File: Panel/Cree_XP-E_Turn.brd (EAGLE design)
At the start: 32 x 20 mm, 5 parts

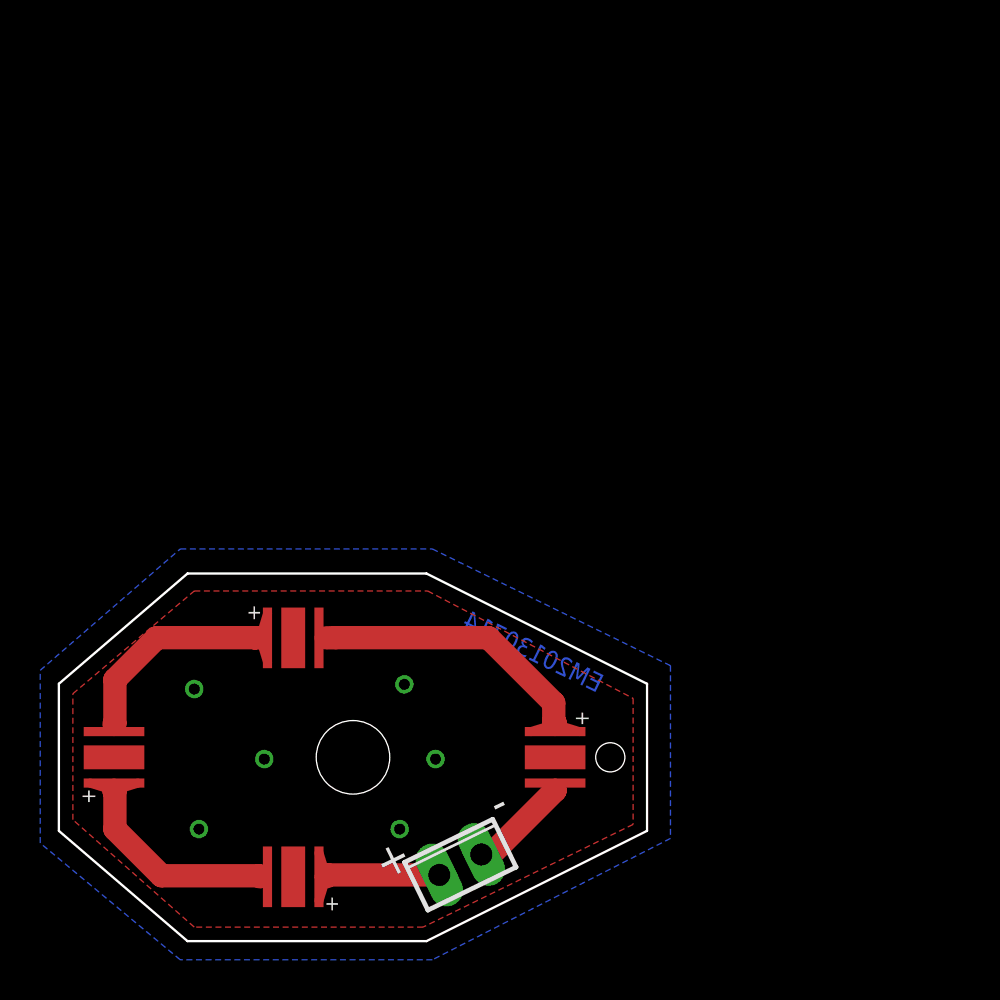
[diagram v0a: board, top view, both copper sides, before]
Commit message: Used Updated XP-E footprint
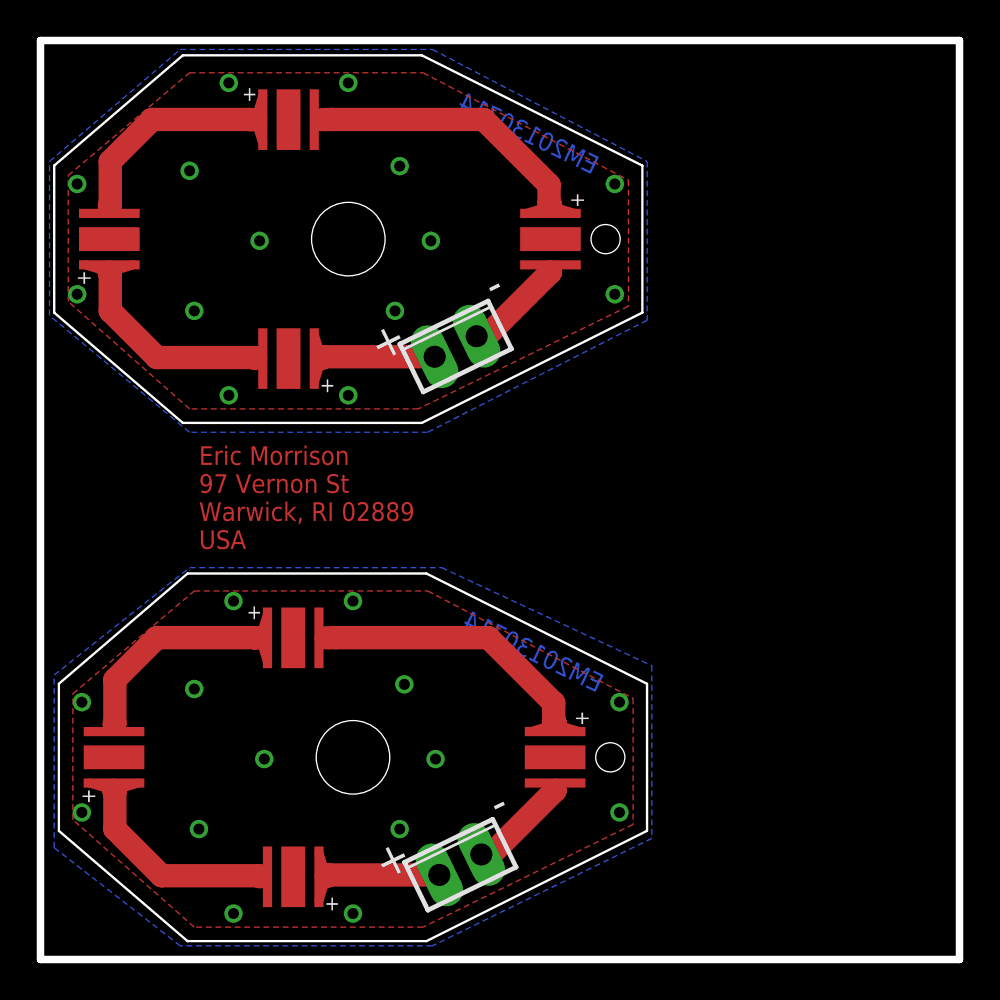
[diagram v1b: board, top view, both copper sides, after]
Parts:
- added LED5, LED6, LED7, LED8: LUXEON_REBELCREE_XP-E, Combined:CREE_XP-E
- added X2: (no value), con-phoenix-254:2POL254
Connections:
- new net N$1: LED5.AN, LED6.CT
- new net N$5: LED6.AN, LED7.CT
- new net N$6: LED7.AN, LED8.CT
- new net THERMAL1: LED5.TH, LED6.TH, LED7.TH, LED8.TH
- new net V+1: LED8.AN, X2.1
- new net V-1: LED5.CT, X2.2
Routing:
- net N$1: track 0.00 -> 15.0 mm
- net N$5: track 0.00 -> 11.3 mm
- net N$6: track 0.00 -> 11.1 mm
- net V+1: track 0.00 -> 6.19 mm
- net V-1: track 0.00 -> 5.46 mm
- added copper zone on layer 1, net THERMAL1
- added copper zone on layer 16, net THERMAL1
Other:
- board size 32 x 20 mm -> 50 x 50 mm
- board text added: "Eric Morrison 97 Vernon St Warwick, RI 02889 USA"
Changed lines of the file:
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@@
 <setting verticaltext="up"/>
 </settings>
-<grid distance="0.01" unitdist="inch" unit="inch" style="lines" multiple="1" display="no" altdistance="0.025" altunitdist="inch" altunit="inch"/>
+<grid distance="0.254" unitdist="mm" unit="mm" style="lines" multiple="1" display="no" altdistance="0.025" altunitdist="inch" altunit="inch"/>
 <layers>
 <layer number="1" name="Top" color="4" fill="1" visible="yes" active="yes"/>
@@
 <text x="29.3" y="13.5" size="1.016" layer="16" rot="MR26">EM20130714</text>
 <hole x="30" y="10" drill="1.5875"/>
+<wire x1="6.746" y1="28.194" x2="-0.254" y2="34.194" width="0.127" layer="20"/>
+<wire x1="-0.254" y1="34.194" x2="-0.254" y2="42.194" width="0.127" layer="20"/>
+<wire x1="-0.254" y1="42.194" x2="6.746" y2="48.194" width="0.127" layer="20"/>
+<wire x1="6.746" y1="48.194" x2="19.746" y2="48.194" width="0.127" layer="20"/>
+<wire x1="19.746" y1="48.194" x2="31.746" y2="42.194" width="0.127" layer="20"/>
+<wire x1="31.746" y1="42.194" x2="31.746" y2="34.194" width="0.127" layer="20"/>
+<wire x1="31.746" y1="34.194" x2="19.746" y2="28.194" width="0.127" layer="20"/>
+<wire x1="19.746" y1="28.194" x2="6.746" y2="28.194" width="0.127" layer="20"/>
+<hole x="15.748" y="38.194" drill="4"/>
+<text x="17.446" y="31.494" size="1.778" layer="21" rot="R26">+</text>
+<text x="23.646" y="34.794" size="1.778" layer="21" rot="R26">-</text>
+<text x="29.046" y="41.694" size="1.016" layer="16" rot="MR26">EM20130714</text>
+<hole x="29.746" y="38.194" drill="1.5875"/>
+<wire x1="-1" y1="-1" x2="49" y2="-1" width="0.4064" layer="20"/>
+<wire x1="49" y1="-1" x2="49" y2="49" width="0.4064" layer="20"/>
+<wire x1="49" y1="49" x2="-1" y2="49" width="0.4064" layer="20"/>
+<wire x1="-1" y1="49" x2="-1" y2="-1" width="0.4064" layer="20"/>
+<text x="7.62" y="21.336" size="1.016" layer="1">Eric Morrison
+97 Vernon St
+Warwick, RI 02889
+USA</text>
 </plain>
 <attributes>
@@
 <attribute name="VALUE" x="20.666921875" y="0.193665625" size="1.27" layer="27" rot="R26"/>
 </element>
+<element name="LED5" library="Combined" package="CREE_XP-E" value="LUXEON_REBELCREE_XP-E" x="26.746" y="38.194" smashed="yes" rot="R270"/>
+<element name="LED6" library="Combined" package="CREE_XP-E" value="LUXEON_REBELCREE_XP-E" x="12.496" y="44.694" smashed="yes"/>
+<element name="LED7" library="Combined" package="CREE_XP-E" value="LUXEON_REBELCREE_XP-E" x="2.746" y="38.194" smashed="yes" rot="R90"/>
+<element name="LED8" library="Combined" package="CREE_XP-E" value="LUXEON_REBELCREE_XP-E" x="12.496" y="31.694" smashed="yes" rot="R180"/>
+<element name="X2" library="con-phoenix-254" package="2POL254" value="" x="21.588" y="32.352" smashed="yes" rot="R26">
+<attribute name="OC_NEWARK" value="unknown" x="64.599721875" y="16.59210625" size="1.778" layer="27" rot="R26" display="off"/>
+<attribute name="MPN" value="" x="64.599721875" y="16.59210625" size="1.778" layer="27" rot="R26" display="off"/>
+<attribute name="MF" value="" x="64.599721875" y="16.59210625" size="1.778" layer="27" rot="R26" display="off"/>
+<attribute name="OC_FARNELL" value="unknown" x="64.599721875" y="16.59210625" size="1.778" layer="27" rot="R26" display="off"/>
+<attribute name="VALUE" x="20.412921875" y="28.387665625" size="1.27" layer="27" rot="R26"/>
+</element>
 </elements>
 <signals>
@@
 </polygon>
 <polygon width="0.254" layer="16">
-<vertex x="-1.016" y="5.334"/>
-<vertex x="-1.016" y="14.732"/>
-<vertex x="6.604" y="21.336"/>
-<vertex x="20.32" y="21.336"/>
-<vertex x="33.274" y="14.986"/>
-<vertex x="33.274" y="5.588"/>
-<vertex x="20.32" y="-1.016"/>
-<vertex x="6.604" y="-1.016"/>
+<vertex x="-0.254" y="5.08"/>
+<vertex x="-0.254" y="14.478"/>
+<vertex x="7.112" y="20.32"/>
+<vertex x="20.828" y="20.32"/>
+<vertex x="32.258" y="14.986"/>
+<vertex x="32.258" y="5.588"/>
+<vertex x="20.32" y="-0.254"/>
+<vertex x="6.604" y="-0.254"/>
 </polygon>
 <via x="7.366" y="13.716" extent="1-16" drill="0.6"/>
@@
 <via x="20.494" y="9.906" extent="1-16" drill="0.6"/>
 <via x="18.542" y="6.096" extent="1-16" drill="0.6"/>
+<via x="30.5" y="13" extent="1-16" drill="0.6"/>
+<via x="30.5" y="7" extent="1-16" drill="0.6"/>
+<via x="9.5" y="18.5" extent="1-16" drill="0.6"/>
+<via x="16" y="18.5" extent="1-16" drill="0.6"/>
+<via x="16" y="1.5" extent="1-16" drill="0.6"/>
+<via x="9.5" y="1.5" extent="1-16" drill="0.6"/>
+<via x="1.25" y="7" extent="1-16" drill="0.6"/>
+<via x="1.25" y="13" extent="1-16" drill="0.6"/>
+</signal>
+<signal name="V-1">
+<contactref element="X2" pad="2"/>
+<contactref element="LED5" pad="CT"/>
+<wire x1="22.729465625" y1="32.90873125" x2="23.25673125" y2="32.90873125" width="1.27" layer="1"/>
+<wire x1="23.25673125" y1="32.90873125" x2="26.742" y2="36.394" width="1.27" layer="1"/>
+<wire x1="26.746" y1="36.394" x2="26.742" y2="36.394" width="1.27" layer="1"/>
+</signal>
+<signal name="N$1">
+<contactref element="LED5" pad="AN"/>
+<contactref element="LED6" pad="CT"/>
+<wire x1="14.296" y1="44.694" x2="14.814" y2="44.704" width="1.27" layer="1"/>
+<wire x1="14.814" y1="44.704" x2="23.114" y2="44.704" width="1.27" layer="1"/>
+<wire x1="23.114" y1="44.704" x2="26.67" y2="41.148" width="1.27" layer="1"/>
+<wire x1="26.67" y1="41.148" x2="26.67" y2="40.132" width="1.27" layer="1"/>
+<wire x1="26.746" y1="39.994" x2="26.746" y2="40.056" width="1.27" layer="1"/>
+<wire x1="26.746" y1="40.056" x2="26.67" y2="40.132" width="1.27" layer="1"/>
+</signal>
+<signal name="N$5">
+<contactref element="LED6" pad="AN"/>
+<contactref element="LED7" pad="CT"/>
+<wire x1="2.746" y1="39.994" x2="2.794" y2="40.042" width="1.27" layer="1"/>
+<wire x1="2.794" y1="40.042" x2="2.794" y2="42.418" width="1.27" layer="1"/>
+<wire x1="2.794" y1="42.418" x2="5.08" y2="44.704" width="1.27" layer="1"/>
+<wire x1="5.08" y1="44.704" x2="10.414" y2="44.704" width="1.27" layer="1"/>
+<wire x1="10.696" y1="44.694" x2="10.424" y2="44.694" width="1.27" layer="1"/>
+<wire x1="10.424" y1="44.694" x2="10.414" y2="44.704" width="1.27" layer="1"/>
+</signal>
+<signal name="N$6">
+<contactref element="LED7" pad="AN"/>
+<contactref element="LED8" pad="CT"/>
+<wire x1="10.696" y1="31.694" x2="10.64" y2="31.75" width="1.27" layer="1"/>
+<wire x1="10.64" y1="31.75" x2="5.334" y2="31.75" width="1.27" layer="1"/>
+<wire x1="5.334" y1="31.75" x2="2.794" y2="34.29" width="1.27" layer="1"/>
+<wire x1="2.794" y1="34.29" x2="2.794" y2="36.322" width="1.27" layer="1"/>
+<wire x1="2.746" y1="36.394" x2="2.746" y2="36.37" width="1.27" layer="1"/>
+<wire x1="2.746" y1="36.37" x2="2.794" y2="36.322" width="1.27" layer="1"/>
+</signal>
+<signal name="V+1">
+<contactref element="LED8" pad="AN"/>
+<contactref element="X2" pad="1"/>
+<wire x1="14.296" y1="31.694" x2="14.397265625" y2="31.795265625" width="1.27" layer="1"/>
+<wire x1="14.397265625" y1="31.795265625" x2="20.44653125" y2="31.795265625" width="1.27" layer="1"/>
+</signal>
+<signal name="THERMAL1">
+<contactref element="LED5" pad="TH"/>
+<contactref element="LED6" pad="TH"/>
+<contactref element="LED7" pad="TH"/>
+<contactref element="LED8" pad="TH"/>
+<polygon width="0.254" layer="1">
+<vertex x="0.508" y="34.798"/>
+<vertex x="0.508" y="41.656"/>
+<vertex x="7.112" y="47.244"/>
+<vertex x="19.812" y="47.244"/>
+<vertex x="30.988" y="41.402"/>
+<vertex x="30.988" y="34.544"/>
+<vertex x="19.558" y="28.956"/>
+<vertex x="7.112" y="28.956"/>
+</polygon>
+<polygon width="0.254" layer="16">
+<vertex x="-0.508" y="34.036"/>
+<vertex x="-0.508" y="42.418"/>
+<vertex x="6.604" y="48.514"/>
+<vertex x="20.32" y="48.514"/>
+<vertex x="32.004" y="42.418"/>
+<vertex x="32.004" y="33.782"/>
+<vertex x="20.066" y="27.686"/>
+<vertex x="7.112" y="27.686"/>
+</polygon>
+<via x="7.112" y="41.91" extent="1-16" drill="0.6"/>
+<via x="18.542" y="42.164" extent="1-16" drill="0.6"/>
+<via x="10.922" y="38.1" extent="1-16" drill="0.6"/>
+<via x="7.366" y="34.29" extent="1-16" drill="0.6"/>
+<via x="20.24" y="38.1" extent="1-16" drill="0.6"/>
+<via x="18.288" y="34.29" extent="1-16" drill="0.6"/>
+<via x="30.246" y="41.194" extent="1-16" drill="0.6"/>
+<via x="30.246" y="35.194" extent="1-16" drill="0.6"/>
+<via x="9.246" y="46.694" extent="1-16" drill="0.6"/>
+<via x="15.746" y="46.694" extent="1-16" drill="0.6"/>
+<via x="15.746" y="29.694" extent="1-16" drill="0.6"/>
+<via x="9.246" y="29.694" extent="1-16" drill="0.6"/>
+<via x="0.996" y="35.194" extent="1-16" drill="0.6"/>
+<via x="0.996" y="41.194" extent="1-16" drill="0.6"/>
 </signal>
 </signals>
 </board>
 </drawing>
+<compatibility>
+<note version="6.3" minversion="6.2.2" severity="warning">
+Since Version 6.2.2 text objects can contain more than one line,
+which will not be processed correctly with this version.
+</note>
+</compatibility>
 </eagle>

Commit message: Turn and Tail combined Panel
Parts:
- added +5V, GND, MEASURE, OUTA, PWM, RESET, TPICLK, TPIDATA: TPI, Personal:TPI_PAD
- added C1: 10n, resistor:C0603
- added C2, C4, C5, C6: .1u, resistor:C0603
- added C3: 47u, resistor:C1206
- added D1: DIODE_0603, Combined:D0603
- added DRILEGEND: (no value), drilegend:DRILEGEND
- added LED10, LED11, LED12, LED9: LUXEON_REBELCREE_XP-E, Combined:CREE_XP-E
- added Q1: SI2301CDS, Combined:SOT-23_POWER
- added Q2: BC846, transistor-neu-to92:SOT23
- added R1: 10k, resistor:R0603
- added R2, R7, R8: 1k, resistor:R0603
- added R3, R4: 3.9k, resistor:R0603
- added R5: .1, resistor:R1206
- added R6: 3.3k, resistor:R0603
- added R9: 28.7K, resistor:R0603
- added U$1: CON_TAILLIGHT, Combined:TAILLIGHT
- added U1: SPX5205M5-L-3-3, Exar_By_element14_Batch_1:SOT95P280X145-5N
- added U2: ATTINY5-TSHR, Atmel_By_element14_Batch_1:SOT95P280X145-6N
- added U3: MCP6L2-X_SN, Combined:SOIC8-N_MC
- moved LED3 0.57 mm to (2.60, 9.60)
- moved LED4 0.57 mm to (12.3, 3.10)
- moved LED1 0.57 mm to (26.6, 9.60)
- moved LED2 0.57 mm to (12.3, 16.1)
- moved X1 0.57 mm to (21.4, 3.76)
- moved X2 0.25 mm to (21.3, 32.4)
- moved LED6 0.25 mm to (12.2, 44.7)
- moved LED8 0.25 mm to (12.2, 31.7)
- moved LED7 0.25 mm to (2.50, 38.2)
- moved LED5 0.25 mm to (26.5, 38.2)
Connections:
- new net +14V: Q1.P$2, R2.1, U$1.H1, U1.1, U1.3
- new net BLINK: R6.1, R7.1, TPICLK.P$1, U2.3
- new net CROSSOVER: LED10.CT, LED11.AN
- new net D-: LED12.CT, R5.2, U3.3
- new net GND: C1.2, C3.2, C4.2, C5.2, C6.2, GND.P$1, LED10.TH, LED11.TH, LED12.TH, LED9.TH, Q2.2, R5.1, R7.2, R8.2, U$1.L1, U$1.L2, U1.2, U2.2, U3.4
- new net INA-: R8.1, R9.2, U3.2
- new net INB+: C4.1, R4.2, U3.5
- new net MEASURE: C2.1, MEASURE.P$1, U2.4, U3.6, U3.7
- new net MOSFET: R1.1, TPIDATA.P$1, U2.1
- new net N$10: C2.2, R3.2, R4.1
- new net N$11: D1.1A, U$1.H2
- new net N$12: D1.2C, R6.2
- new net N$13: LED11.CT, LED12.AN
- new net N$14: LED9.AN, Q1.P$3
- new net N$15: LED10.AN, LED9.CT
- new net N$7: C1.1, U1.4
- new net N$8: PWM.P$1, Q1.P$1, Q2.3, R2.2
- new net N$9: Q2.1, R1.2
- new net OUTA: OUTA.P$1, R3.1, R9.1, U3.1
- new net RESET: RESET.P$1, U2.6
- new net VCC: +5V.P$1, C3.1, C5.1, C6.1, U1.5, U2.5, U3.8
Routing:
- net VCC: track 0.00 -> 15.1 mm
- net MEASURE: track 0.00 -> 13.4 mm
- net D-: track 0.00 -> 12.4 mm
- net +14V: track 0.00 -> 12.4 mm
- net OUTA: track 0.00 -> 11.7 mm
- net MOSFET: track 0.00 -> 10.9 mm, vias 0 -> 2
- net N$11: track 0.00 -> 10.2 mm, vias 0 -> 1
- net CROSSOVER: track 0.00 -> 9.60 mm
- net N$10: track 0.00 -> 8.52 mm
- net BLINK: track 0.00 -> 6.13 mm
- net N$9: track 0.00 -> 5.47 mm
- net N$8: track 0.00 -> 5.36 mm
- net N$14: track 0.00 -> 4.97 mm
- net N$15: track 0.00 -> 4.76 mm, vias 0 -> 1
- net INB+: track 0.00 -> 4.38 mm
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- added copper zone on layer 1, net +14V
- added copper zone on layer 1, net GND
- added copper zone on layer 16, net GND
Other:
- outline, holes or cut-outs redrawn
- board text added: "C"
- board text added: "C1"
- board text added: "C2"
- board text added: "C3"
- board text added: "C4"
- board text added: "C5"
- board text added: "C6"
- board text added: "D"
- board text added: "D1"
- board text added: "EWM 20130716 BULB RETROFIT"
- board text added: "G"
- board text added: "M"
- board text added: "Q1"
- board text added: "Q2"
- board text added: "R"
- board text added: "R1"
- board text added: "R2"
- board text added: "R3"
- board text added: "R4"
- board text added: "R5"
- board text added: "R6"
- board text added: "R7"
- board text added: "R8"
- board text added: "R9"
- board text added: "U1"
- board text added: "U2"
- board text added: "U3"
- board text added: "V"

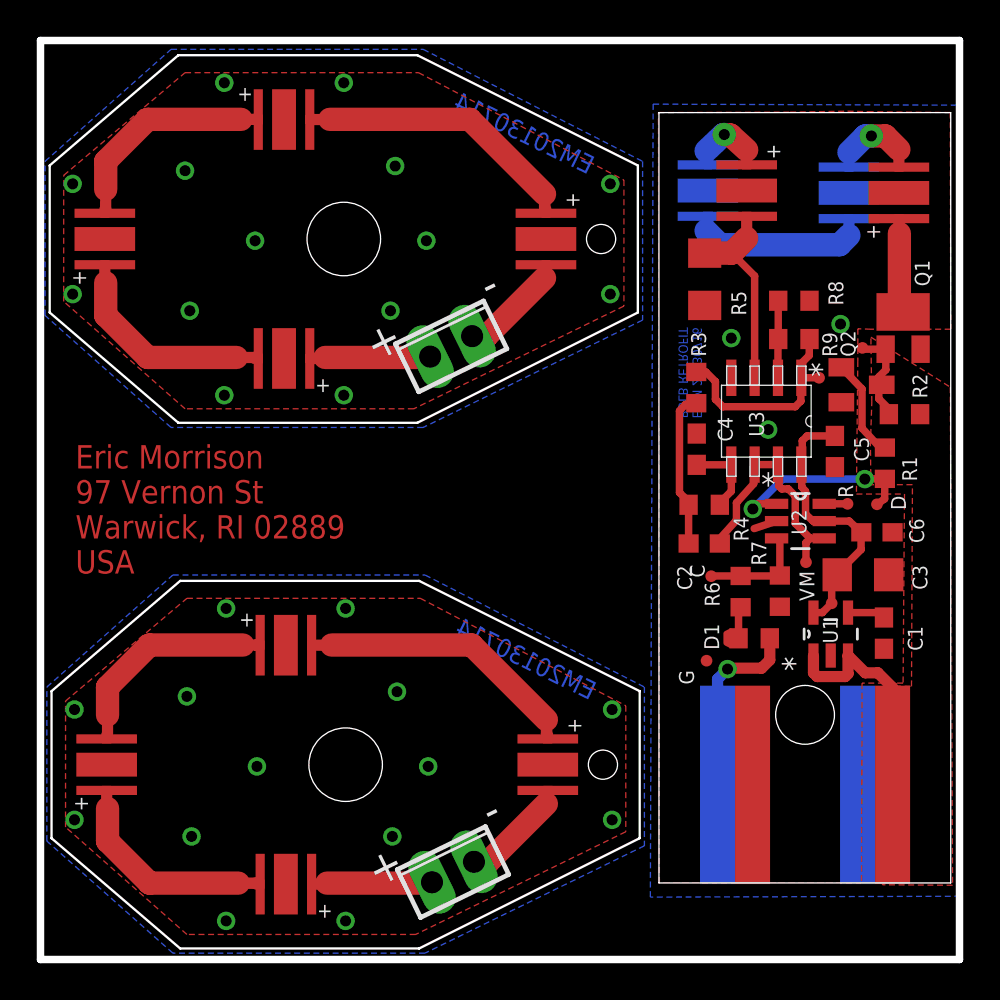
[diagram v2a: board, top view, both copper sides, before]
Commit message: updated tail board in combined panel
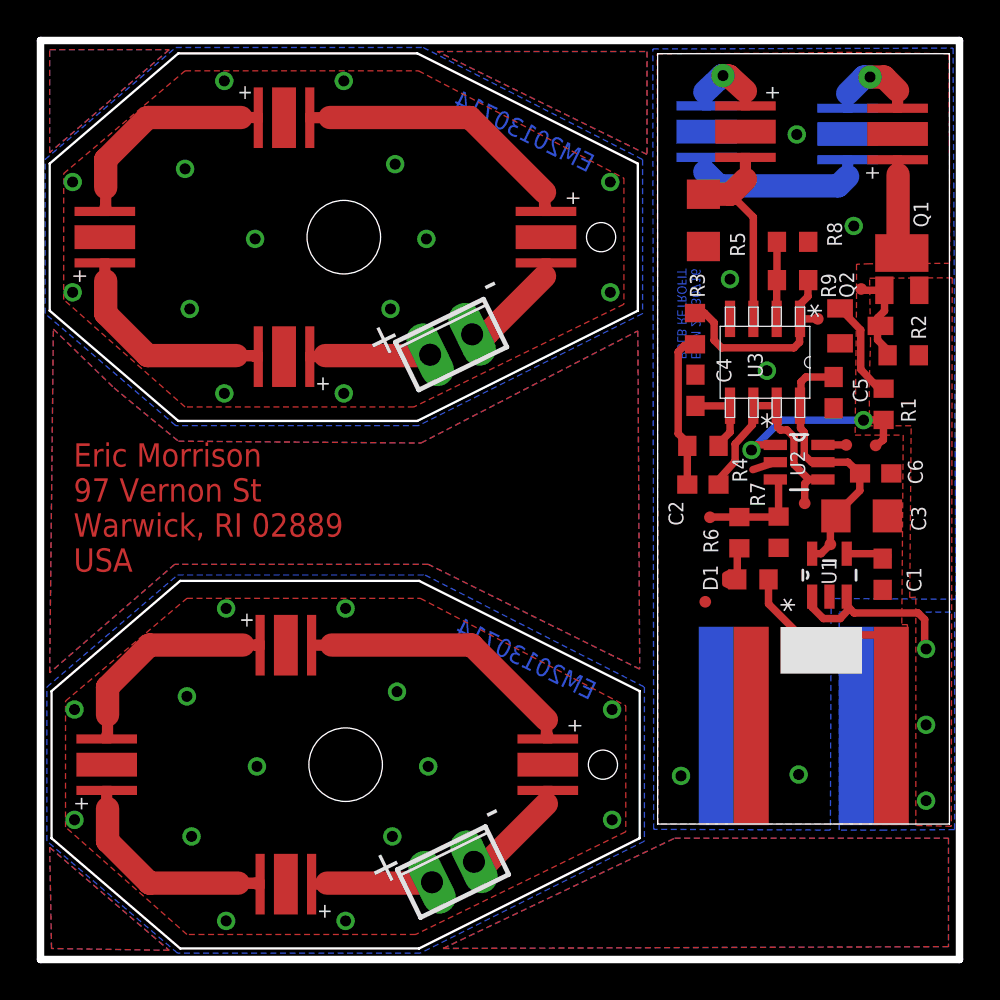
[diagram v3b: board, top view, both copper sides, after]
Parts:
- moved LED10 3.21 mm to (42.9, 43.9)
- moved LED9 3.21 mm to (45.6, 43.9)
- moved PWM 3.21 mm to (43.7, 35.5)
- moved +5V 3.21 mm to (42.0, 21.6)
- moved C2 3.21 mm to (35.0, 24.8)
- moved C5 3.21 mm to (42.2, 29.8)
- moved MEASURE 3.21 mm to (40.6, 23.8)
- moved R1 3.21 mm to (44.9, 29.2)
- moved R2 3.21 mm to (45.9, 31.9)
- moved R4 3.21 mm to (35.0, 26.9)
- moved R7 3.21 mm to (39.2, 22.2)
- moved RESET 3.21 mm to (42.8, 27.0)
- moved U1 3.21 mm to (41.9, 19.9)
- moved GND 3.21 mm to (35.2, 18.5)
- moved U$1 3.21 mm to (40.5, 11.7)
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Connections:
- net +14V: now also U$1.L1; no longer U$1.H1
- net GND: now also U$1.H2; no longer U$1.L1
- net N$11: now also U$1.H1; no longer U$1.H2
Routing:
- net N$11: track 10.2 -> 13.6 mm, vias 1 -> 0
- net +14V: track 12.4 -> 9.79 mm, vias 0 -> 3
- net GND: vias 3 -> 6
- added copper zone on layer 16, net +14V
- added copper zone on layer 1, net S$1
- added copper zone on layer 16, net S$1
- added copper zone on layer 1, net S$2
- added copper zone on layer 16, net S$2
- added copper zone on layer 1, net S$3
- added copper zone on layer 16, net S$3
- added copper zone on layer 1, net S$4
- added copper zone on layer 16, net S$4
- added copper zone on layer 1, net S$5
- added copper zone on layer 16, net S$5
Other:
- outline, holes or cut-outs redrawn
